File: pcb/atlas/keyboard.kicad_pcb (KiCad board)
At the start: 2 copper layers, 242 x 96 mm, 104 parts, among them SW1 SW_Push, SW10 SW_Push, SW11 SW_Push, SW12 SW_Push, SW13 SW_Push, SW14 SW_Push, SW15 SW_Push, SW16 SW_Push, SW17 SW_Push, SW18 SW_Push, SW19 SW_Push, SW2 SW_Push, SW20 SW_Push, SW21 SW_Push, SW22 SW_Push, SW23 SW_Push, SW24 SW_Push, SW25 SW_Push, SW26 SW_Push, SW27 SW_Push, SW28 SW_Push, SW29 SW_Push, SW3 SW_Push, SW30 SW_Push, SW31 SW_Push, SW32 SW_Push, SW33 SW_Push, SW34 SW_Push, SW4 SW_Push, SW5 SW_Push, SW6 SW_Push, SW7 SW_Push, SW8 SW_Push, SW9 SW_Push

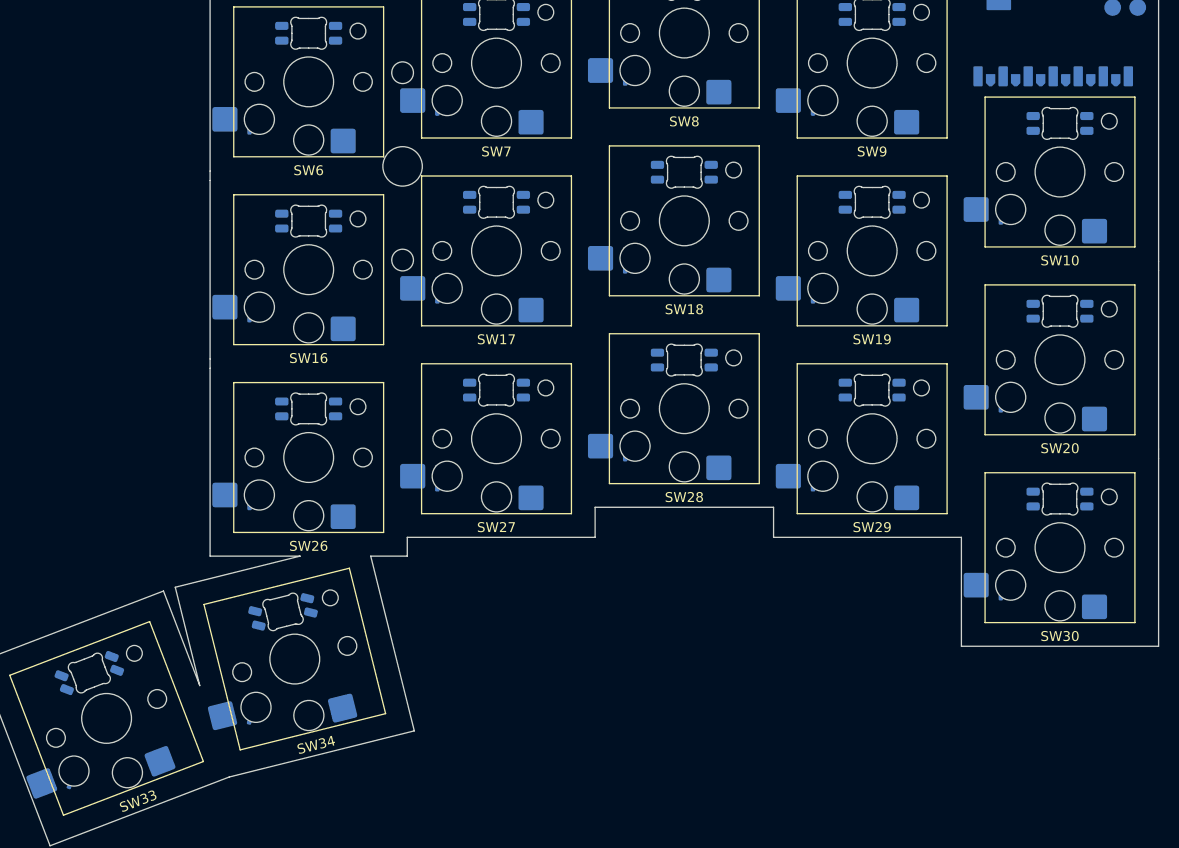
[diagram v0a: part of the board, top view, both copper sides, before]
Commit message: fix(pcb): mirror diodes by switch-local pose, not centerline
Centerline-mirroring diodes put each right-half diode at x'=2·center−x —
which inverts its X offset relative to its parent switch. With switches at
rotation 180° on both halves, a left diode at switch+(+6, +4) ended up at
switch+(−6, +4) on the right — visually the diode jumped to the opposite
side of the switch.

mirror_to_right.py now uses two passes:
  - centerline mirror for Edge.Cuts + free-placed footprints (MCU, etc.)
  - switch-local re-pair for diodes: anchor each left diode to its
    nearest left switch, lift to that switch's local frame, then place
    a copy at the paired right switch using the same local pose.

The switch ↔ switch pairing uses mirror position (each left switch's
partner is the right switch closest to 2·center−x, y).

After re-run, D3 and D3_R both sit at offset (+6, +4) from their
respective switches.
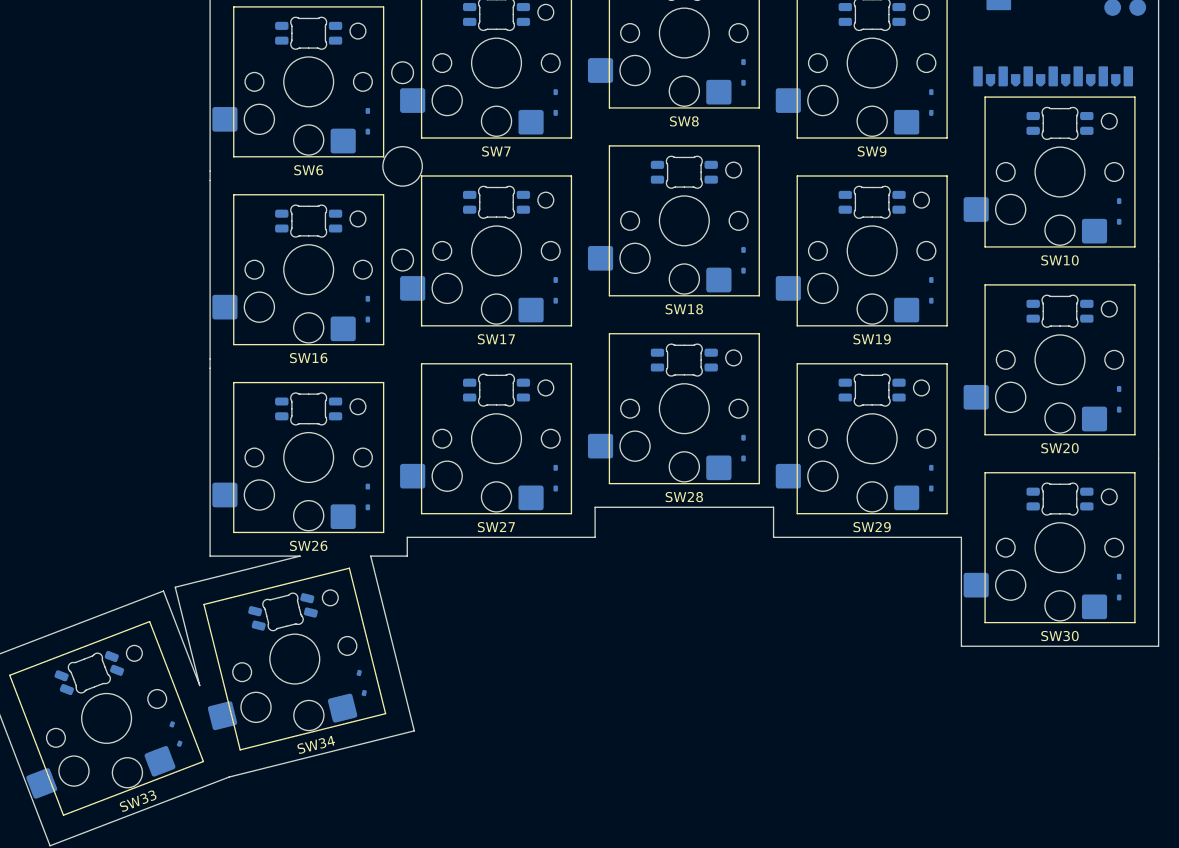
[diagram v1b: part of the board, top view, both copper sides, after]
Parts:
- moved D31_R 12.0 mm to (187.4, 117.0)
- moved D13_R 12.0 mm to (226.2, 74.1)
- moved D23_R 12.0 mm to (226.2, 93.1)
- moved D3_R 12.0 mm to (226.2, 55.0)
- moved D11_R 12.0 mm to (264.3, 88.2)
- moved D12_R 12.0 mm to (245.2, 77.1)
- moved D14_R 12.0 mm to (207.1, 77.1)
- moved D15_R 12.0 mm to (188.1, 79.0)
- moved D1_R 12.0 mm to (264.3, 69.1)
- moved D21_R 12.0 mm to (264.3, 107.2)
- moved D22_R 12.0 mm to (245.2, 96.2)
- moved D24_R 12.0 mm to (207.1, 96.2)
- moved D5_R 12.0 mm to (188.1, 60.0)
- moved D25_R 12.0 mm to (188.1, 98.1)
- moved D2_R 12.0 mm to (245.2, 58.1)
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
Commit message: fix(pcb): split right-half nets — atlas is BT, halves aren't wired
kbplacer hands out a single shared matrix net list. For a wired split that's
fine; for atlas (each half a standalone BLE peripheral) the row nets MUST
NOT span the centerline, otherwise KiCad draws ratlines between halves and
the netlist implies the boards are electrically joined.

mirror_to_right.py now runs a third pass after the position fixes:

  - ROW{n} → R_ROW{n} on every right-half footprint pad
    (kbplacer already splits COL{n} per half, so columns are untouched).
  - On every right-half diode (D{n}_R), rename its anode net from the
    inherited Net-(D{n}-A) to Net-(D{n}_R-A).
  - On every right-half switch, rewrite the dangling anode-net reference
    (which still pointed at a now-deleted kbplacer diode) to the new
    Net-(D{n}_R-A) of its physically-paired right-half diode.

After this, SW2↔D2 on the left and SW9↔D2_R on the right have their own
disjoint Net-(...-A) and ROW nets.
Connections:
- D11_R pad 1: ROW1 -> R_ROW1
- D11_R pad 2: Net-(D11-A) -> Net-(D11_R-A)
- D12_R pad 1: ROW1 -> R_ROW1
- D12_R pad 2: Net-(D12-A) -> Net-(D12_R-A)
- D13_R pad 1: ROW1 -> R_ROW1
- D13_R pad 2: Net-(D13-A) -> Net-(D13_R-A)
- D14_R pad 1: ROW1 -> R_ROW1
- D14_R pad 2: Net-(D14-A) -> Net-(D14_R-A)
- D15_R pad 1: ROW1 -> R_ROW1
- D15_R pad 2: Net-(D15-A) -> Net-(D15_R-A)
- D1_R pad 1: ROW0 -> R_ROW0
- D1_R pad 2: Net-(D1-A) -> Net-(D1_R-A)
- D21_R pad 1: ROW2 -> R_ROW2
- D21_R pad 2: Net-(D21-A) -> Net-(D21_R-A)
- D22_R pad 1: ROW2 -> R_ROW2
- D22_R pad 2: Net-(D22-A) -> Net-(D22_R-A)
- D23_R pad 1: ROW2 -> R_ROW2
- D23_R pad 2: Net-(D23-A) -> Net-(D23_R-A)
- D24_R pad 1: ROW2 -> R_ROW2
- D24_R pad 2: Net-(D24-A) -> Net-(D24_R-A)
- D25_R pad 1: ROW2 -> R_ROW2
- D25_R pad 2: Net-(D25-A) -> Net-(D25_R-A)
- D2_R pad 1: ROW0 -> R_ROW0
- D2_R pad 2: Net-(D2-A) -> Net-(D2_R-A)
- D31_R pad 1: ROW3 -> R_ROW3
- D31_R pad 2: Net-(D31-A) -> Net-(D31_R-A)
- D32_R pad 1: ROW3 -> R_ROW3
- D32_R pad 2: Net-(D32-A) -> Net-(D32_R-A)
- D3_R pad 1: ROW0 -> R_ROW0
- D3_R pad 2: Net-(D3-A) -> Net-(D3_R-A)
- D4_R pad 1: ROW0 -> R_ROW0
- D4_R pad 2: Net-(D4-A) -> Net-(D4_R-A)
- D5_R pad 1: ROW0 -> R_ROW0
- D5_R pad 2: Net-(D5-A) -> Net-(D5_R-A)
- SW10 pad 2: Net-(D10-A) -> Net-(D1_R-A)
- SW16 pad 2: Net-(D16-A) -> Net-(D15_R-A)
- SW17 pad 2: Net-(D17-A) -> Net-(D14_R-A)
- SW18 pad 2: Net-(D18-A) -> Net-(D13_R-A)
- SW19 pad 2: Net-(D19-A) -> Net-(D12_R-A)
- SW20 pad 2: Net-(D20-A) -> Net-(D11_R-A)
- SW26 pad 2: Net-(D26-A) -> Net-(D25_R-A)
- SW27 pad 2: Net-(D27-A) -> Net-(D24_R-A)
- SW28 pad 2: Net-(D28-A) -> Net-(D23_R-A)
- SW29 pad 2: Net-(D29-A) -> Net-(D22_R-A)
- SW30 pad 2: Net-(D30-A) -> Net-(D21_R-A)
- SW33 pad 2: Net-(D33-A) -> Net-(D32_R-A)
- SW34 pad 2: Net-(D34-A) -> Net-(D31_R-A)
- SW6 pad 2: Net-(D6-A) -> Net-(D5_R-A)
- SW7 pad 2: Net-(D7-A) -> Net-(D4_R-A)
- SW8 pad 2: Net-(D8-A) -> Net-(D3_R-A)
- SW9 pad 2: Net-(D9-A) -> Net-(D2_R-A)
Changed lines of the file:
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@@
 			(layers "B.Cu" "B.Mask" "B.Paste")
 			(roundrect_rratio 0.1)
-			(net "Net-(D7-A)")
+			(net "Net-(D4_R-A)")
 			(pinfunction "2")
 		)
@@
 			(layers "B.Cu" "B.Mask" "B.Paste")
 			(roundrect_rratio 0.1)
-			(net "Net-(D6-A)")
+			(net "Net-(D5_R-A)")
 			(pinfunction "2")
 		)
@@
 			(layers "B.Cu" "B.Mask" "B.Paste")
 			(roundrect_rratio 0.1)
-			(net "Net-(D17-A)")
+			(net "Net-(D14_R-A)")
 			(pinfunction "2")
 		)
@@
 			(layers "B.Cu" "B.Mask" "B.Paste")
 			(roundrect_rratio 0.1)
-			(net "Net-(D26-A)")
+			(net "Net-(D25_R-A)")
 			(pinfunction "2")
 		)
@@
 			(layers "B.Cu" "B.Mask" "B.Paste")
 			(roundrect_rratio 0.1)
-			(net "Net-(D28-A)")
+			(net "Net-(D23_R-A)")
 			(pinfunction "2")
 		)
@@
 			(layers "B.Cu" "B.Mask" "B.Paste")
 			(roundrect_rratio 0.1)
-			(net "Net-(D8-A)")
+			(net "Net-(D3_R-A)")
 			(pinfunction "2")
 		)
@@
 			(layers "B.Cu" "B.Mask" "B.Paste")
 			(roundrect_rratio 0.1)
-			(net "Net-(D9-A)")
+			(net "Net-(D2_R-A)")
 			(pinfunction "2")
 		)
@@
 			(layers "B.Cu" "B.Mask" "B.Paste")
 			(roundrect_rratio 0.1)
-			(net "Net-(D19-A)")
+			(net "Net-(D12_R-A)")
 			(pinfunction "2")
 		)
@@
 			(layers "B.Cu" "B.Mask" "B.Paste")
 			(roundrect_rratio 0.1)
-			(net "Net-(D18-A)")
+			(net "Net-(D13_R-A)")
 			(pinfunction "2")
 		)
@@
 			(layers "B.Cu" "B.Mask" "B.Paste")
 			(roundrect_rratio 0.1)
-			(net "Net-(D16-A)")
+			(net "Net-(D15_R-A)")
 			(pinfunction "2")
 		)
@@
 			(layers "B.Cu" "B.Mask" "B.Paste")
 			(roundrect_rratio 0.1)
-			(net "Net-(D20-A)")
+			(net "Net-(D11_R-A)")
 			(pinfunction "2")
 		)
@@
 			(layers "B.Cu" "B.Mask" "B.Paste")
 			(roundrect_rratio 0.1)
-			(net "Net-(D33-A)")
+			(net "Net-(D32_R-A)")
 			(pinfunction "2")
 		)
@@
 			(layers "B.Cu" "B.Mask" "B.Paste")
 			(roundrect_rratio 0.1)
-			(net "Net-(D29-A)")
+			(net "Net-(D22_R-A)")
 			(pinfunction "2")
 		)
@@
 			(layers "B.Cu" "B.Mask" "B.Paste")
 			(roundrect_rratio 0.1)
-			(net "Net-(D30-A)")
+			(net "Net-(D21_R-A)")
 			(pinfunction "2")
 		)
@@
 			(layers "B.Cu" "B.Mask" "B.Paste")
 			(roundrect_rratio 0.1)
-			(net "Net-(D34-A)")
+			(net "Net-(D31_R-A)")
 			(pinfunction "2")
 		)
@@
 			(layers "B.Cu" "B.Mask" "B.Paste")
 			(roundrect_rratio 0.1)
-			(net "Net-(D10-A)")
+			(net "Net-(D1_R-A)")
 			(pinfunction "2")
 		)
@@
 			(layers "B.Cu" "B.Mask" "B.Paste")
 			(roundrect_rratio 0.1)
-			(net "Net-(D27-A)")
+			(net "Net-(D24_R-A)")
 			(pinfunction "2")
 		)
@@
 			(layers "B.Cu" "B.Mask" "B.Paste")
 			(roundrect_rratio 0.25)
-			(net "ROW2")
+			(net "R_ROW2")
 			(pinfunction "K")
 		)
@@
 			(layers "B.Cu" "B.Mask" "B.Paste")
 			(roundrect_rratio 0.25)
-			(net "Net-(D25-A)")
+			(net "Net-(D25_R-A)")
 			(pinfunction "A")
 		)
@@
 			(layers "B.Cu" "B.Mask" "B.Paste")
 			(roundrect_rratio 0.25)
-			(net "ROW0")
+			(net "R_ROW0")
 			(pinfunction "K")
 		)
@@
 			(layers "B.Cu" "B.Mask" "B.Paste")
 			(roundrect_rratio 0.25)
-			(net "Net-(D2-A)")
+			(net "Net-(D2_R-A)")
 			(pinfunction "A")
 		)
@@
 			(layers "B.Cu" "B.Mask" "B.Paste")
 			(roundrect_rratio 0.25)
-			(net "ROW0")
+			(net "R_ROW0")
 			(pinfunction "K")
 		)
@@
 			(layers "B.Cu" "B.Mask" "B.Paste")
 			(roundrect_rratio 0.25)
-			(net "Net-(D5-A)")
+			(net "Net-(D5_R-A)")
 			(pinfunction "A")
 		)
@@
 			(layers "B.Cu" "B.Mask" "B.Paste")
 			(roundrect_rratio 0.25)
-			(net "ROW0")
+			(net "R_ROW0")
 			(pinfunction "K")
 		)
@@
 			(layers "B.Cu" "B.Mask" "B.Paste")
 			(roundrect_rratio 0.25)
-			(net "Net-(D4-A)")
+			(net "Net-(D4_R-A)")
 			(pinfunction "A")
 		)
@@
 			(layers "B.Cu" "B.Mask" "B.Paste")
 			(roundrect_rratio 0.25)
-			(net "ROW0")
+			(net "R_ROW0")
 			(pinfunction "K")
 		)
@@
 			(layers "B.Cu" "B.Mask" "B.Paste")
 			(roundrect_rratio 0.25)
-			(net "Net-(D1-A)")
+			(net "Net-(D1_R-A)")
 			(pinfunction "A")
 		)
@@
 			(layers "B.Cu" "B.Mask" "B.Paste")
 			(roundrect_rratio 0.25)
-			(net "ROW2")
+			(net "R_ROW2")
 			(pinfunction "K")
 		)
@@
 			(layers "B.Cu" "B.Mask" "B.Paste")
 			(roundrect_rratio 0.25)
-			(net "Net-(D24-A)")
+			(net "Net-(D24_R-A)")
 			(pinfunction "A")
 		)
@@
 			(layers "B.Cu" "B.Mask" "B.Paste")
 			(roundrect_rratio 0.25)
-			(net "ROW1")
+			(net "R_ROW1")
 			(pinfunction "K")
 		)
@@
 			(layers "B.Cu" "B.Mask" "B.Paste")
 			(roundrect_rratio 0.25)
-			(net "Net-(D11-A)")
+			(net "Net-(D11_R-A)")
 			(pinfunction "A")
 		)
@@
 			(layers "B.Cu" "B.Mask" "B.Paste")
 			(roundrect_rratio 0.25)
-			(net "ROW3")
+			(net "R_ROW3")
 			(pinfunction "K")
 		)
@@
 			(layers "B.Cu" "B.Mask" "B.Paste")
 			(roundrect_rratio 0.25)
-			(net "Net-(D32-A)")
+			(net "Net-(D32_R-A)")
 			(pinfunction "A")
 		)
@@
 			(layers "B.Cu" "B.Mask" "B.Paste")
 			(roundrect_rratio 0.25)
-			(net "ROW1")
+			(net "R_ROW1")
 			(pinfunction "K")
 		)
@@
 			(layers "B.Cu" "B.Mask" "B.Paste")
 			(roundrect_rratio 0.25)
-			(net "Net-(D15-A)")
+			(net "Net-(D15_R-A)")
 			(pinfunction "A")
 		)
@@
 			(layers "B.Cu" "B.Mask" "B.Paste")
 			(roundrect_rratio 0.25)
-			(net "ROW3")
+			(net "R_ROW3")
 			(pinfunction "K")
 		)
@@
 			(layers "B.Cu" "B.Mask" "B.Paste")
 			(roundrect_rratio 0.25)
-			(net "Net-(D31-A)")
+			(net "Net-(D31_R-A)")
 			(pinfunction "A")
 		)
@@
 			(layers "B.Cu" "B.Mask" "B.Paste")
 			(roundrect_rratio 0.25)
-			(net "ROW2")
+			(net "R_ROW2")
 			(pinfunction "K")
 		)
@@
 			(layers "B.Cu" "B.Mask" "B.Paste")
 			(roundrect_rratio 0.25)
-			(net "Net-(D22-A)")
+			(net "Net-(D22_R-A)")
 			(pinfunction "A")
 		)
@@
 			(layers "B.Cu" "B.Mask" "B.Paste")
 			(roundrect_rratio 0.25)
-			(net "ROW0")
+			(net "R_ROW0")
 			(pinfunction "K")
 		)
@@
 			(layers "B.Cu" "B.Mask" "B.Paste")
 			(roundrect_rratio 0.25)
-			(net "Net-(D3-A)")
+			(net "Net-(D3_R-A)")
 			(pinfunction "A")
 		)
@@
 			(layers "B.Cu" "B.Mask" "B.Paste")
 			(roundrect_rratio 0.25)
-			(net "ROW1")
+			(net "R_ROW1")
 			(pinfunction "K")
 		)
@@
 			(layers "B.Cu" "B.Mask" "B.Paste")
 			(roundrect_rratio 0.25)
-			(net "Net-(D14-A)")
+			(net "Net-(D14_R-A)")
 			(pinfunction "A")
 		)
@@
 			(layers "B.Cu" "B.Mask" "B.Paste")
 			(roundrect_rratio 0.25)
-			(net "ROW2")
+			(net "R_ROW2")
 			(pinfunction "K")
 		)
@@
 			(layers "B.Cu" "B.Mask" "B.Paste")
 			(roundrect_rratio 0.25)
-			(net "Net-(D21-A)")
+			(net "Net-(D21_R-A)")
 			(pinfunction "A")
 		)
@@
 			(layers "B.Cu" "B.Mask" "B.Paste")
 			(roundrect_rratio 0.25)
-			(net "ROW1")
+			(net "R_ROW1")
 			(pinfunction "K")
 		)
@@
 			(layers "B.Cu" "B.Mask" "B.Paste")
 			(roundrect_rratio 0.25)
-			(net "Net-(D12-A)")
+			(net "Net-(D12_R-A)")
 			(pinfunction "A")
 		)
@@
 			(layers "B.Cu" "B.Mask" "B.Paste")
 			(roundrect_rratio 0.25)
-			(net "ROW1")
+			(net "R_ROW1")
 			(pinfunction "K")
 		)
@@
 			(layers "B.Cu" "B.Mask" "B.Paste")
 			(roundrect_rratio 0.25)
-			(net "Net-(D13-A)")
+			(net "Net-(D13_R-A)")
 			(pinfunction "A")
 		)
@@
 			(layers "B.Cu" "B.Mask" "B.Paste")
 			(roundrect_rratio 0.25)
-			(net "ROW2")
+			(net "R_ROW2")
 			(pinfunction "K")
 		)
@@
 			(layers "B.Cu" "B.Mask" "B.Paste")
 			(roundrect_rratio 0.25)
-			(net "Net-(D23-A)")
+			(net "Net-(D23_R-A)")
 			(pinfunction "A")
 		)
